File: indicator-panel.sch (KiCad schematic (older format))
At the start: 72 parts, among them P101 CONN_01X08, P102 CONN_01X08, P103 CONN_01X04, P104 CONN_01X04, U101 MAX3294, U102 STP16CP05, U103 STP16CP05, U106 STP16CP05, U108 LD1117S33CTR, U109 MAX3280, U110 MAX3280, U111 MAX3280

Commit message: Fix up connectors to carry current.
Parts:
- removed P101: CONN_01X08, Pin_Headers:Pin_Header_Angled_2x04, symbol CONN_01X08
- removed P102: CONN_01X08, Socket_Strips:Socket_Strip_Angled_2x04, symbol CONN_01X08
- removed P103: CONN_01X04, Pin_Headers:Pin_Header_Angled_1x04, symbol CONN_01X04
- removed P104: CONN_01X04, Socket_Strips:Socket_Strip_Angled_1x04, symbol CONN_01X04
- added P101: CONN_01X06, Pin_Headers:Pin_Header_Angled_2x03, symbol CONN_01X06
- added P102: CONN_01X06, Socket_Strips:Socket_Strip_Angled_2x03, symbol CONN_01X06
- added P103: CONN_01X08, Pin_Headers:Pin_Header_Angled_2x04, symbol CONN_01X08
- added P104: CONN_01X08, Socket_Strips:Socket_Strip_Angled_2x04, symbol CONN_01X08
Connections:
- wire segments 231 -> 229
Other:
- moved on the sheet: U110, U111

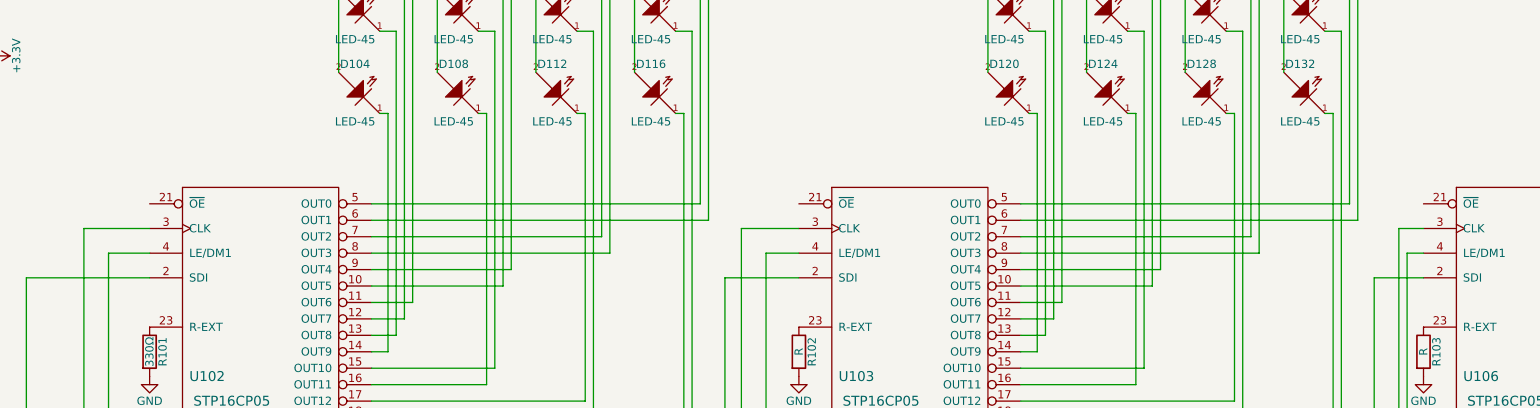
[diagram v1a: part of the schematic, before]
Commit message: Cleaned up schematic and added RK inlay.
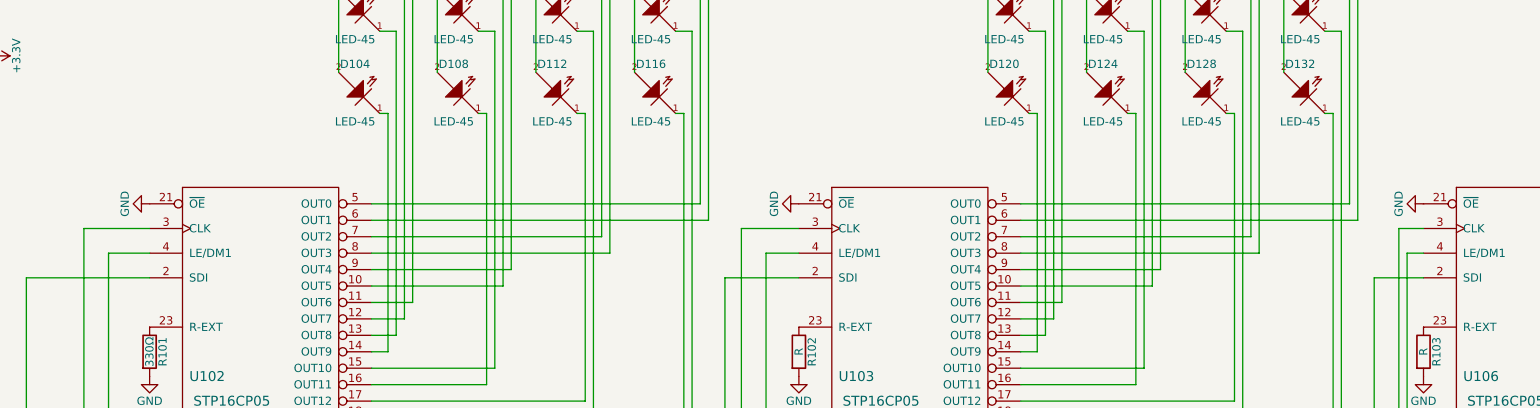
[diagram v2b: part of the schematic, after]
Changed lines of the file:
@@
 	-1   0    0    -1
 $EndComp
+$Comp
+L GND #PWR?
+U 1 1 562144CC
+P 4650 4000
+F 0 "#PWR?" H 4650 3750 50  0001 C CNN
+F 1 "GND" H 4650 3850 50  0000 C CNN
+F 2 "" H 4650 4000 60  0000 C CNN
+F 3 "" H 4650 4000 60  0000 C CNN
+	1    4650 4000
+	0    1    1    0
+$EndComp
+$Comp
+L GND #PWR?
+U 1 1 562145AF
+P 8600 4000
+F 0 "#PWR?" H 8600 3750 50  0001 C CNN
+F 1 "GND" H 8600 3850 50  0000 C CNN
+F 2 "" H 8600 4000 60  0000 C CNN
+F 3 "" H 8600 4000 60  0000 C CNN
+	1    8600 4000
+	0    1    1    0
+$EndComp
+$Comp
+L GND #PWR?
+U 1 1 56214692
+P 12400 4000
+F 0 "#PWR?" H 12400 3750 50  0001 C CNN
+F 1 "GND" H 12400 3850 50  0000 C CNN
+F 2 "" H 12400 4000 60  0000 C CNN
+F 3 "" H 12400 4000 60  0000 C CNN
+	1    12400 4000
+	0    1    1    0
+$EndComp
 $EndSCHEMATC

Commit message: Updated pcb and rk11 inlay to .44x.88 spacing.
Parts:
- removed P101: CONN_01X06, Pin_Headers:Pin_Header_Angled_2x03, symbol CONN_01X06
- removed P102: CONN_01X06, Socket_Strips:Socket_Strip_Angled_2x03, symbol CONN_01X06
- removed P103: CONN_01X08, Pin_Headers:Pin_Header_Angled_2x04, symbol CONN_01X08
- removed P104: CONN_01X08, Socket_Strips:Socket_Strip_Angled_2x04, symbol CONN_01X08
- added P101: CONN_01X08, Pin_Headers:Pin_Header_Angled_2x04, symbol CONN_01X08
- added P102: CONN_01X08, Socket_Strips:Socket_Strip_Angled_2x04, symbol CONN_01X08
- added P103: CONN_01X10, Pin_Headers:Pin_Header_Angled_2x05, symbol CONN_01X10
- added P104: CONN_01X10, Socket_Strips:Socket_Strip_Angled_2x05, symbol CONN_01X10
- D101, D102, D103, D104, D105, D106, D107, D108, D109, D110, D111, D112, D113, D114, D115, D116, D117, D118, D119, D120, D121, D122, D123, D124, D125, D126, D127, D128, D129, D130, D131, D132, D133, D134, D135, D136, D137, D138, D139, D140, D141, D142, D143, D144, D145, D146, D147, D148: footprint LEDs:LED-1206 -> myMods.pretty:LED_SMDuniversal_0805to1206
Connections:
- no-connect marks 0 -> 4

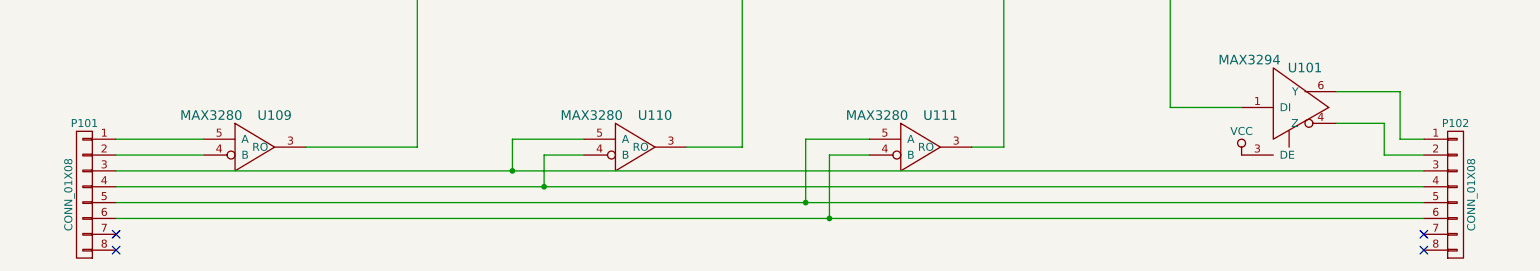
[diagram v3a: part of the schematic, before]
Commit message: Changed data connector use so it can be reversed with no harm.  Updated version to 1.1.
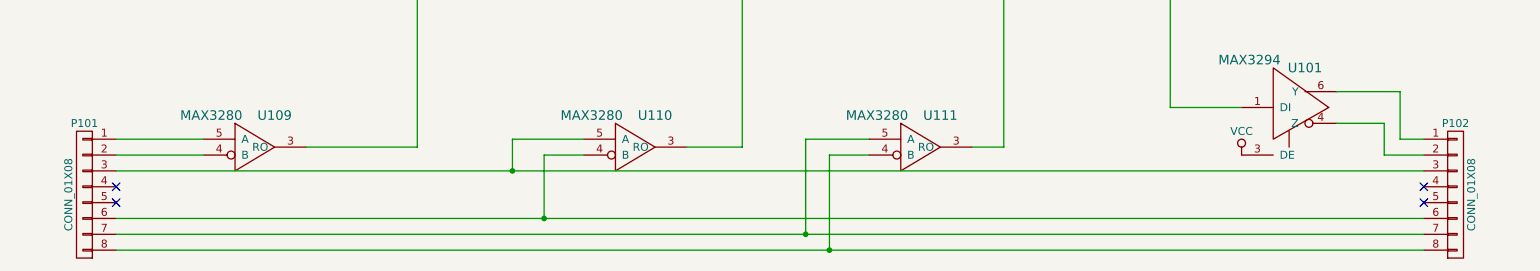
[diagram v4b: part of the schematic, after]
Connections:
- net at P101.6 (P6), P102.6 (P6): now also U110.4 (B); no longer U111.4 (B)
- net at P101.7 (P7): now also P102.7 (P7), U111.5 (A)
- net at P101.8 (P8): now also P102.8 (P8), U111.4 (B)
- now unconnected: P101.4 (P4), P101.5 (P5), P102.4 (P4), P102.5 (P5)
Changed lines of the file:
@@
 encoding utf-8
 Sheet 1 1
-Title ""
-Date ""
-Rev ""
-Comp ""
+Title "Indicator Panel"
+Date "2015-12-21"
+Rev "1.1"
+Comp "Vintage Computer Engineering"
 Comment1 ""
 Comment2 ""
@@
 	2000 7500 10250 7500
 Wire Wire Line
-	2000 7600 10250 7600
-Wire Wire Line
-	2000 7700 10250 7700
-Wire Wire Line
-	2000 7800 10250 7800
-Wire Wire Line
 	4500 7500 4500 7300
 Wire Wire Line
@@
 Connection ~ 4500 7500
 Wire Wire Line
-	4700 7600 4700 7400
+	4700 7800 4700 7400
 Wire Wire Line
 	4700 7400 4950 7400
-Connection ~ 4700 7600
+Connection ~ 4700 7800
 Wire Wire Line
 	6750 7400 6500 7400
 Wire Wire Line
-	6500 7400 6500 7800
-Connection ~ 6500 7800
+	6500 7400 6500 8000
+Connection ~ 6500 8000
 Wire Wire Line
 	6750 7300 6350 7300
 Wire Wire Line
-	6350 7300 6350 7700
-Connection ~ 6350 7700
+	6350 7300 6350 7900
+Connection ~ 6350 7900
 Wire Wire Line
 	5600 7350 5950 7350
@@
 	1    0    0    -1
 $EndComp
-NoConn ~ 10250 7900
-NoConn ~ 10250 8000
-NoConn ~ 2000 7900
-NoConn ~ 2000 8000
+NoConn ~ 10250 7600
+NoConn ~ 10250 7700
+NoConn ~ 2000 7700
+Wire Wire Line
+	2000 7900 10250 7900
+Wire Wire Line
+	2000 8000 10250 8000
+Wire Wire Line
+	2000 7800 10250 7800
+NoConn ~ 2000 7600
 $EndSCHEMATC

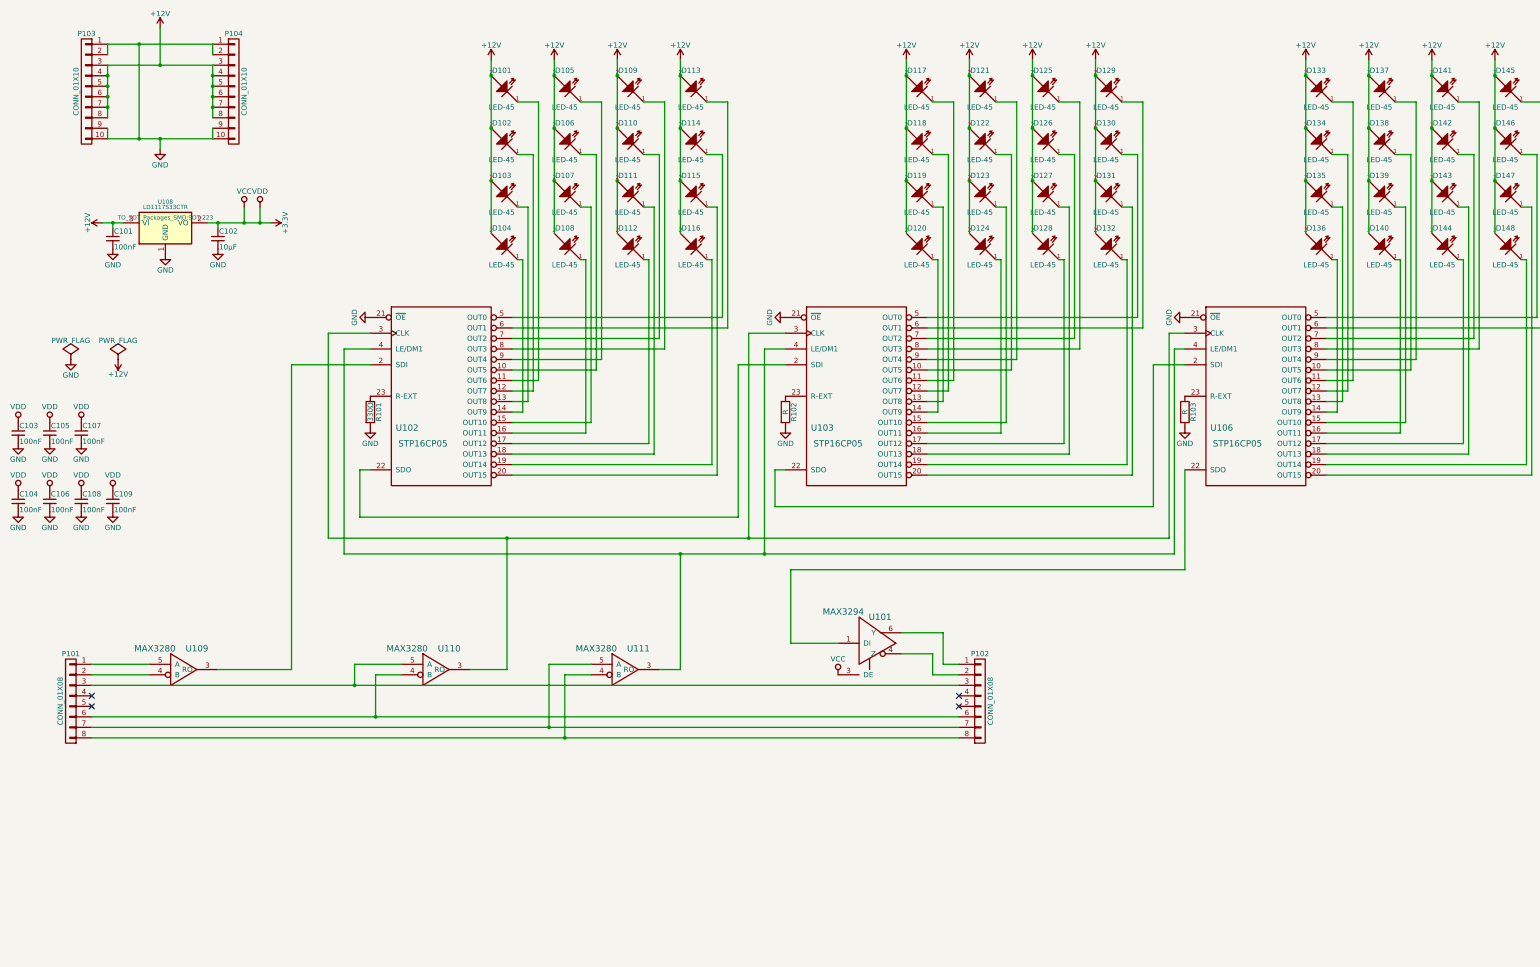
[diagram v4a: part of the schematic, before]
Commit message: Added barrel connector.
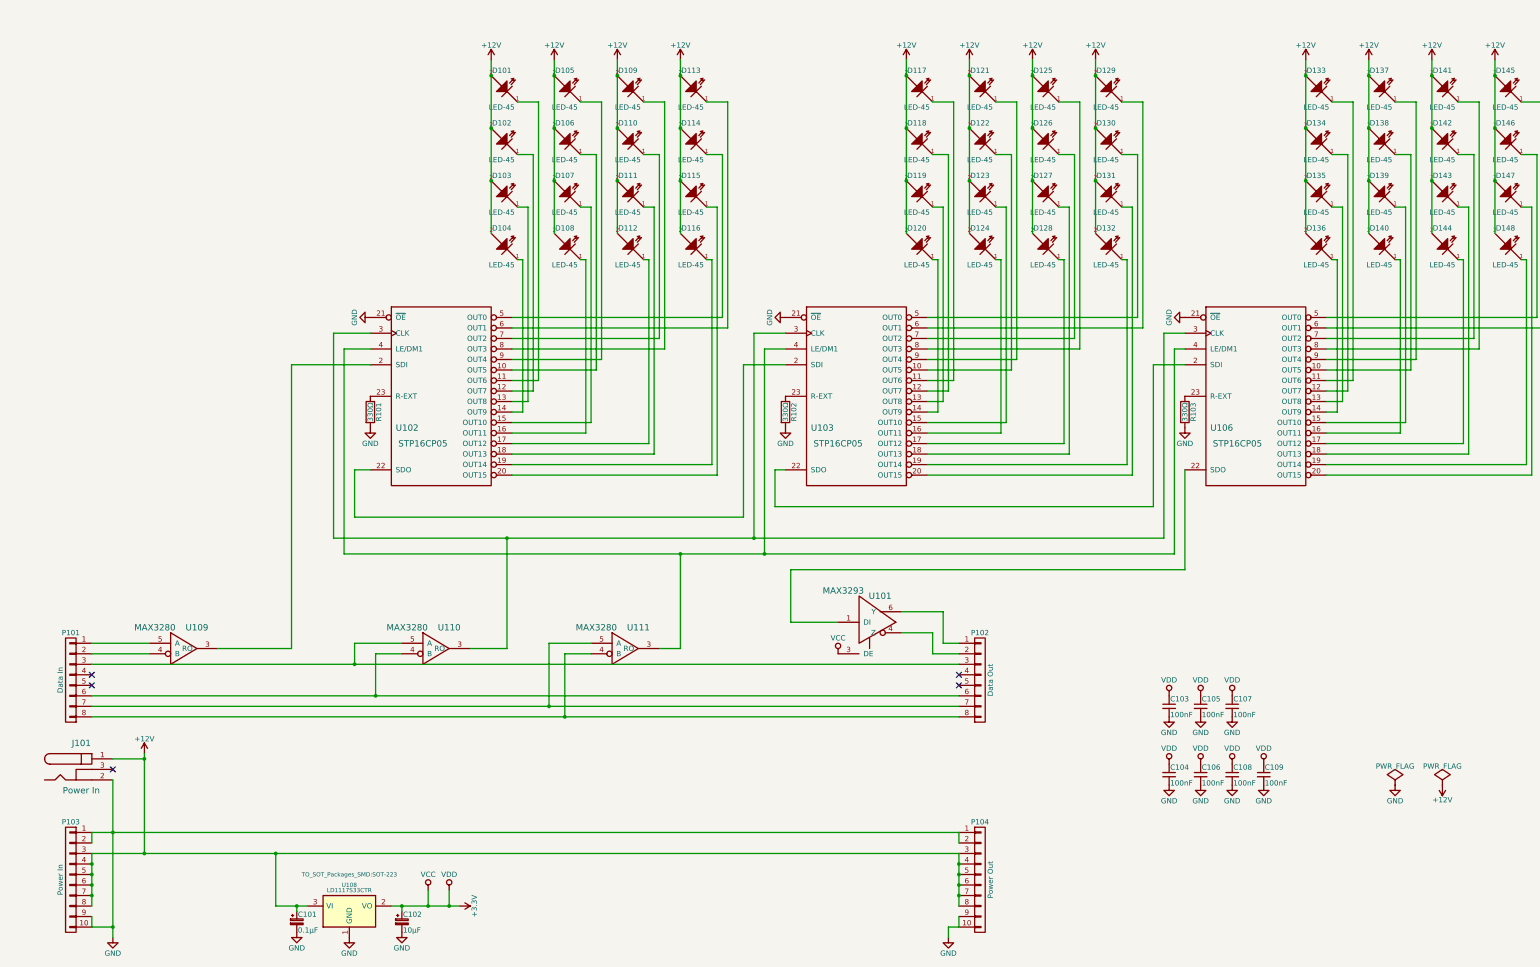
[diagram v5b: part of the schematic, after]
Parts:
- removed C101: 100nF, Capacitors_SMD:C_0805_HandSoldering, symbol C_Small
- removed C102: 10μF, Capacitors_SMD:C_0805_HandSoldering, symbol C_Small
- added C101: 0.1μF, Capacitors_SMD:C_0805, symbol CP_Small
- added C102: 10μF, Capacitors_SMD:C_0805, symbol CP_Small
- added J101: Power In, Connect:BARREL_JACK, symbol BARREL_JACK
- P101: value CONN_01X08 -> Data In
- P102: value CONN_01X08 -> Data Out
- P103: value CONN_01X10 -> Power In
- P104: value CONN_01X10 -> Power Out
- R102, R103: value R -> 330Ω
- U101: value MAX3294 -> MAX3293
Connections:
- net +12V: now also C101.1, J101.1
- net +3V3: now also C102.1
- net GND: now also C101.2, C102.2, J101.2
- no-connect marks 4 -> 5
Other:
- moved on the sheet: C103, C104, C105, C106, C107, C108, C109, P101, P102, P103, P104, U101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

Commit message: Added barrel connector and shrunk schematic to Letter size.  Last update before changing to add Blank and Board Detect signals.
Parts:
- C101: footprint Capacitors_SMD:C_0805 -> Capacitors_Tantalum_SMD:TantalC_SizeR_EIA-2012; manf# (none) -> TAJR104K020RNJ
- C102: footprint Capacitors_SMD:C_0805 -> Capacitors_Tantalum_SMD:TantalC_SizeR_EIA-2012; manf# (none) -> TPSP106M010R2000
- C103: manf# (none) -> C0805C104K3RACT
- D101: manf# (none) -> QBLP631-IW
- P101, P102: manf# (none) -> 68021-208HLF
- P103, P104: manf# (none) -> 68021-210HLF
- R102: manf# (none) -> RC0805FR-07330RL
- U101: manf# (none) -> MAX3293AUT+T
- U102, U103, U106: manf# (none) -> STP16CP05MTR
- U108: manf# (none) -> LD1117S33CTR
- U109, U110, U111: manf# (none) -> MAX3280EAUK+T
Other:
- moved on the sheet: C101, C102, C103, C104, C105, C106, C107, C108, C109, D101, D102, D103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
